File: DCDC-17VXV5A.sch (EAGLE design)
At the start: 36 parts, among them Q10 NMOSFET, Q9 NMOSFET, U1 LM3150MHX/NOPB

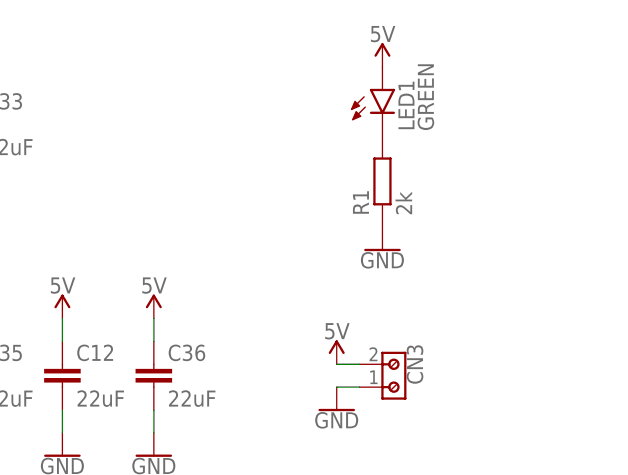
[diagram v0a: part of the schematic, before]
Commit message: Changed LEDs resistor. Generated CAM filers. Generated PNG preview. Generated PDF schematics. Updated description.
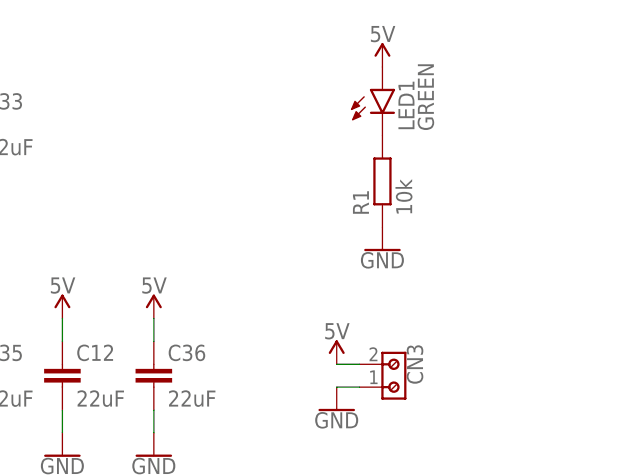
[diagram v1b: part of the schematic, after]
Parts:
- R1: value 2k -> 10k
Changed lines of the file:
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@@
 <part name="LOGO2" library="_my_logos" deviceset="MFDECLOGO" device="_L_10MM" value="MFDECLOGO_L_10MM"/>
 <part name="LED1" library="led" library_urn="urn:adsk.eagle:library:259" deviceset="LED" device="SML0603" package3d_urn="urn:adsk.eagle:package:15832/1" value="GREEN"/>
-<part name="R1" library="rcl" library_urn="urn:adsk.eagle:library:334" deviceset="R-EU_" device="R0603" package3d_urn="urn:adsk.eagle:package:23555/3" value="2k"/>
+<part name="R1" library="rcl" library_urn="urn:adsk.eagle:library:334" deviceset="R-EU_" device="R0603" package3d_urn="urn:adsk.eagle:package:23555/3" value="10k"/>
 <part name="SUPPLY7" library="SparkFun-PowerSymbols" library_urn="urn:adsk.eagle:library:530" deviceset="5V" device=""/>
 <part name="GND4" library="SparkFun-PowerSymbols" library_urn="urn:adsk.eagle:library:530" deviceset="GND" device=""/>
